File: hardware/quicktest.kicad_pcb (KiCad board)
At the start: 2 copper layers, 36 x 30 mm, 48 parts, among them J1 USB_OTG, J2 Vibration Motor, J3 CONN_02X03, Q1 PMOS_2.5A/30V, Q2 2N2222, SW1 SW_Push, SW2 SW_Push, SW3 SW_Push, U1 DS3231MZ, U2 ATMEGA328P-AU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

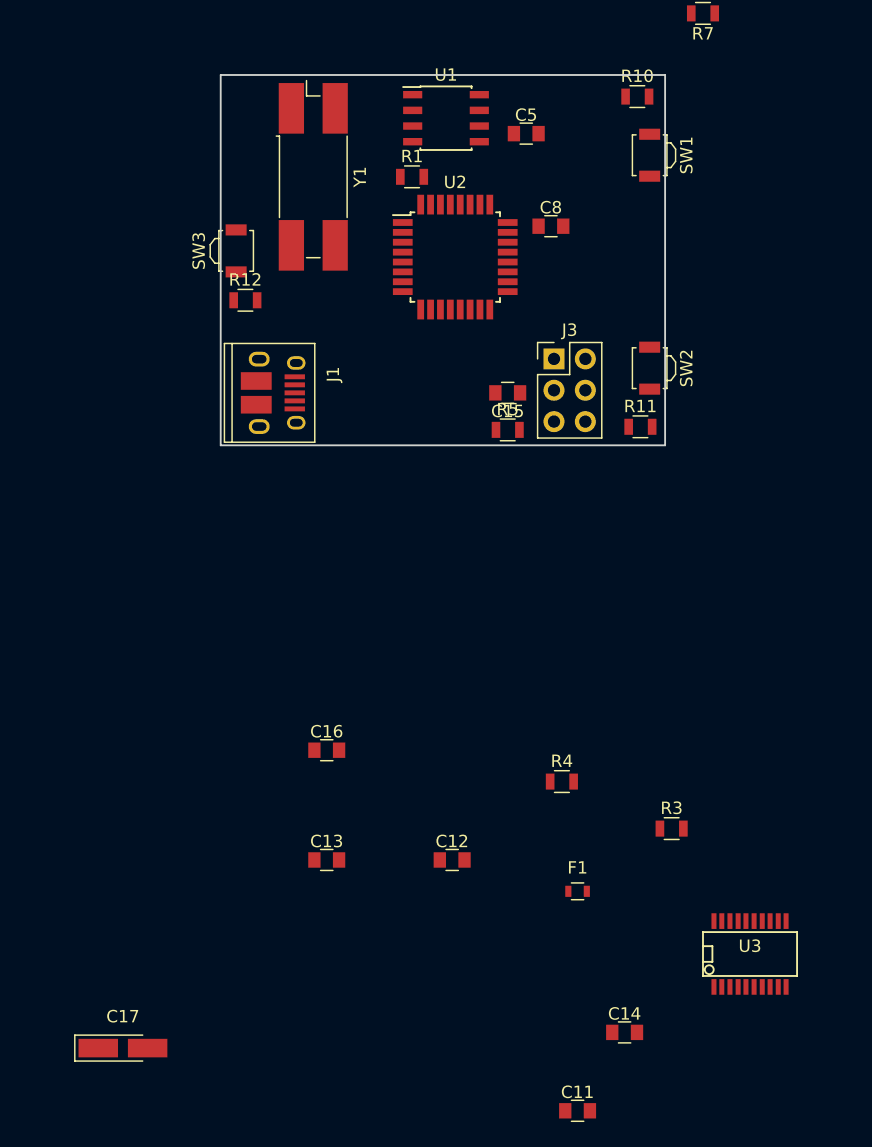
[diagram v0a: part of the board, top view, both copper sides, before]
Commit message: decided to start with a light version of the watch, have been working on that schematic and pcb
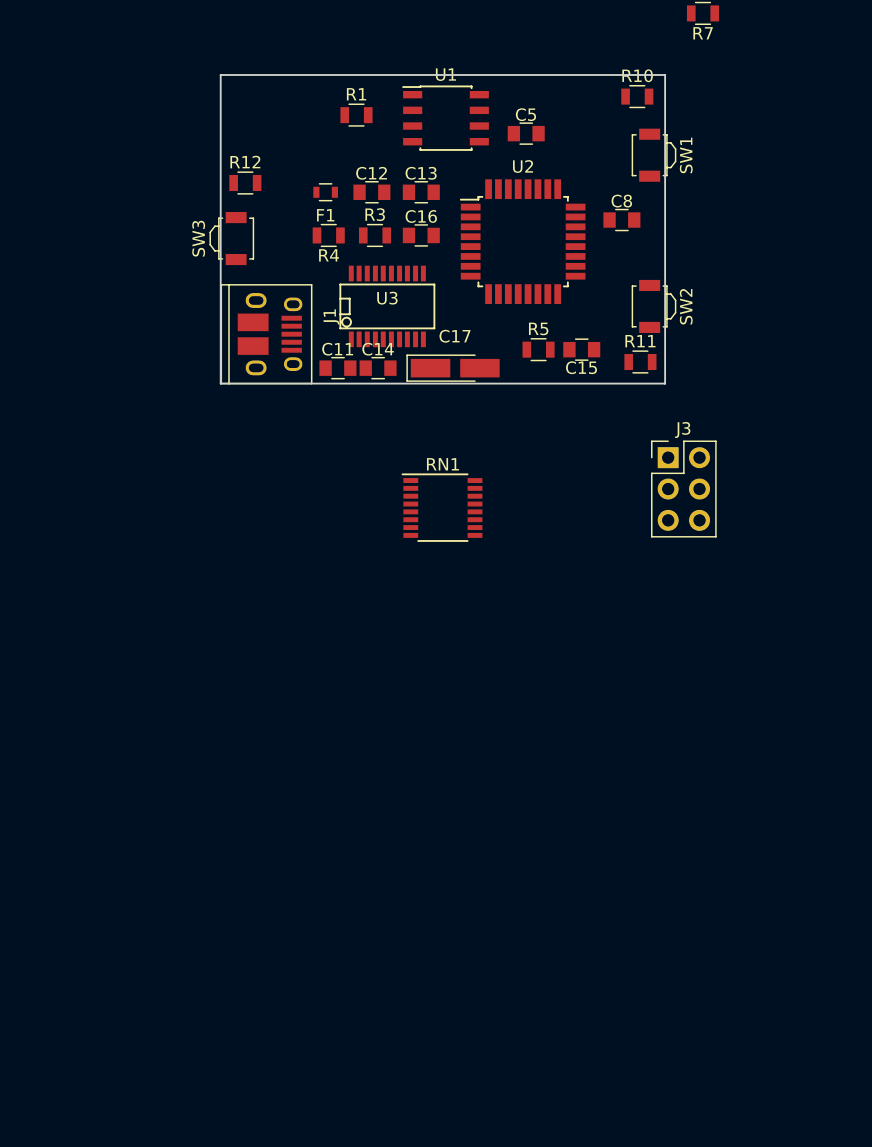
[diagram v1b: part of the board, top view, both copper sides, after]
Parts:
- removed Y1: 8MHz, Crystals:Crystal_SMD_SeikoEpson_MA506-4pin_12.7x5.1mm
- added RN1: R_Network_8, Housings_SSOP:SSOP-16_3.9x4.9mm_Pitch0.635mm, F.Cu at (158.0, 120.1)
- moved C11 63.2 mm to (149.5, 108.8)
- moved C17 61.3 mm to (159.0, 108.8)
- moved F1 60.2 mm to (148.5, 94.5), turned to 180 degrees
- moved U3 60.1 mm to (153.5, 103.8)
- moved C14 57.4 mm to (152.8, 108.8)
- moved C13 54.6 mm to (156.2, 94.5)
- moved C12 54.5 mm to (152.2, 94.5)
- moved R3 53.7 mm to (152.5, 98.0)
- moved R4 48.1 mm to (148.8, 98.0), turned to 180 degrees
- moved C16 42.4 mm to (156.2, 98.0)
- moved J3 12.2 mm to (176.2, 116.0)
- moved R12 9.50 mm to (142.0, 93.8)
- moved R5 6.96 mm to (165.8, 107.2)
- moved C15 6.95 mm to (169.2, 107.2)
- moved R1 6.73 mm to (151.0, 88.2)
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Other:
- board size 36 x 30 mm -> 36 x 25 mm
